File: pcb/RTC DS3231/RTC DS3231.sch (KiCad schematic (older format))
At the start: 9 parts

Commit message: Updated schematic.
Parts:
- added D101: LED, symbol Device:LED
- added D102: D, symbol Device:D
- added R101: 1k, symbol Device:R
- added R102: 200, symbol Device:R
- added RN101: 4.7K, Resistor_THT:R_Array_SIP5, symbol Device:R_Network04_US
- RN102: renamed from RN?; value R_Network04_US -> 4.7K
- gave numbers to parts that had none: 8
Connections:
- net GND: now also BT101.2 (-), J101.6 (Pin_6), J102.4 (Pin_4), JP101.1, JP102.1, JP103.1, U102.7 (WP), D101.1 (K)
- net VCC: now also J101.5 (Pin_5), J102.3 (Pin_3), RN102.1 (common), R101.1, R102.1, RN101.1 (common)
- net 32KHZ: now reaches U101.1 (32KHZ)
- net 32KHZ: now also J101.1 (Pin_1), RN102.5 (R4)
- net VBAT: now reaches U101.14 (VBAT)
- net VBAT: now also BT101.1 (+), D102.1 (K)
- net SDA: now reaches U101.15 (SDA)
- net SDA: now also J101.4 (Pin_4), J102.2 (Pin_2), RN102.2 (R1), U102.6 (SCL)
- net SCL: now reaches U101.16 (SCL)
- net SCL: now also J101.3 (Pin_3), J102.1 (Pin_1), RN102.3 (R2), U102.5 (SDA)
- net SQW: now reaches U101.3 (~INT~/SQW)
- net SQW: now also J101.2 (Pin_2), RN102.4 (R3)
- net at U102.1 (A0): now also JP101.2, RN101.5 (R4)
- net at U102.2 (A1): now also JP102.2, RN101.4 (R3)
- net at U102.3 (A2): now also JP103.2, RN101.3 (R2)
- new net: D101.2 (A), R101.2
- new net: D102.2 (A), R102.2
- no-connect marks 0 -> 2
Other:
- note added: "Battery Charge Circuit"
- moved on the sheet: BT101, J101, J102, JP101, JP102, JP103, RN102, U102

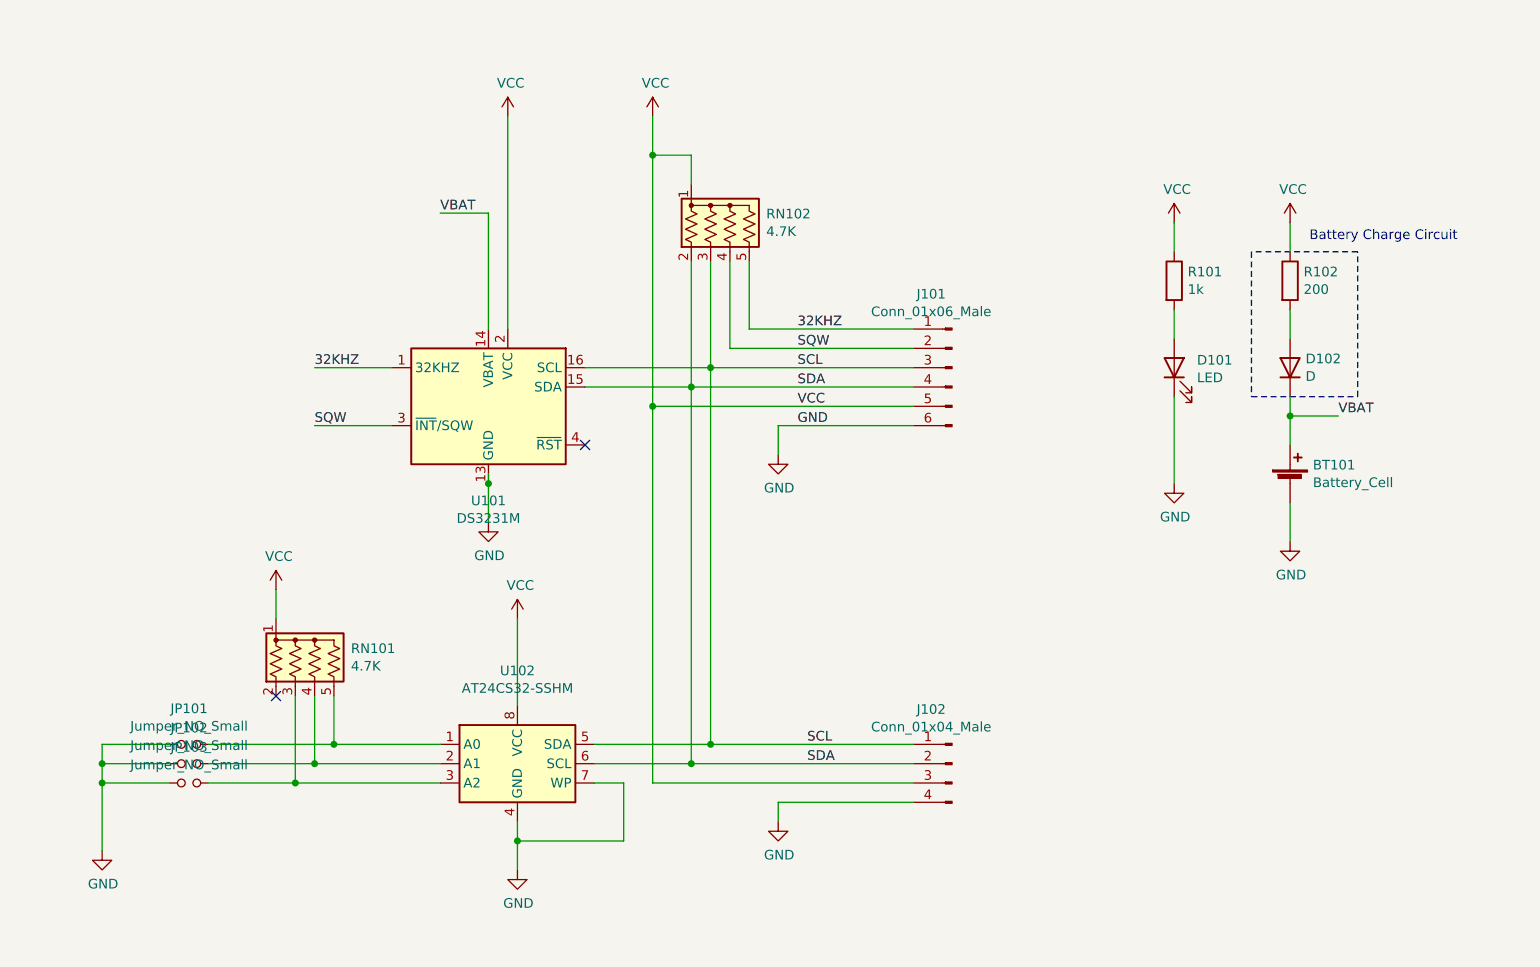
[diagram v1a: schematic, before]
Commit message: Updates schematic to pass ERC.
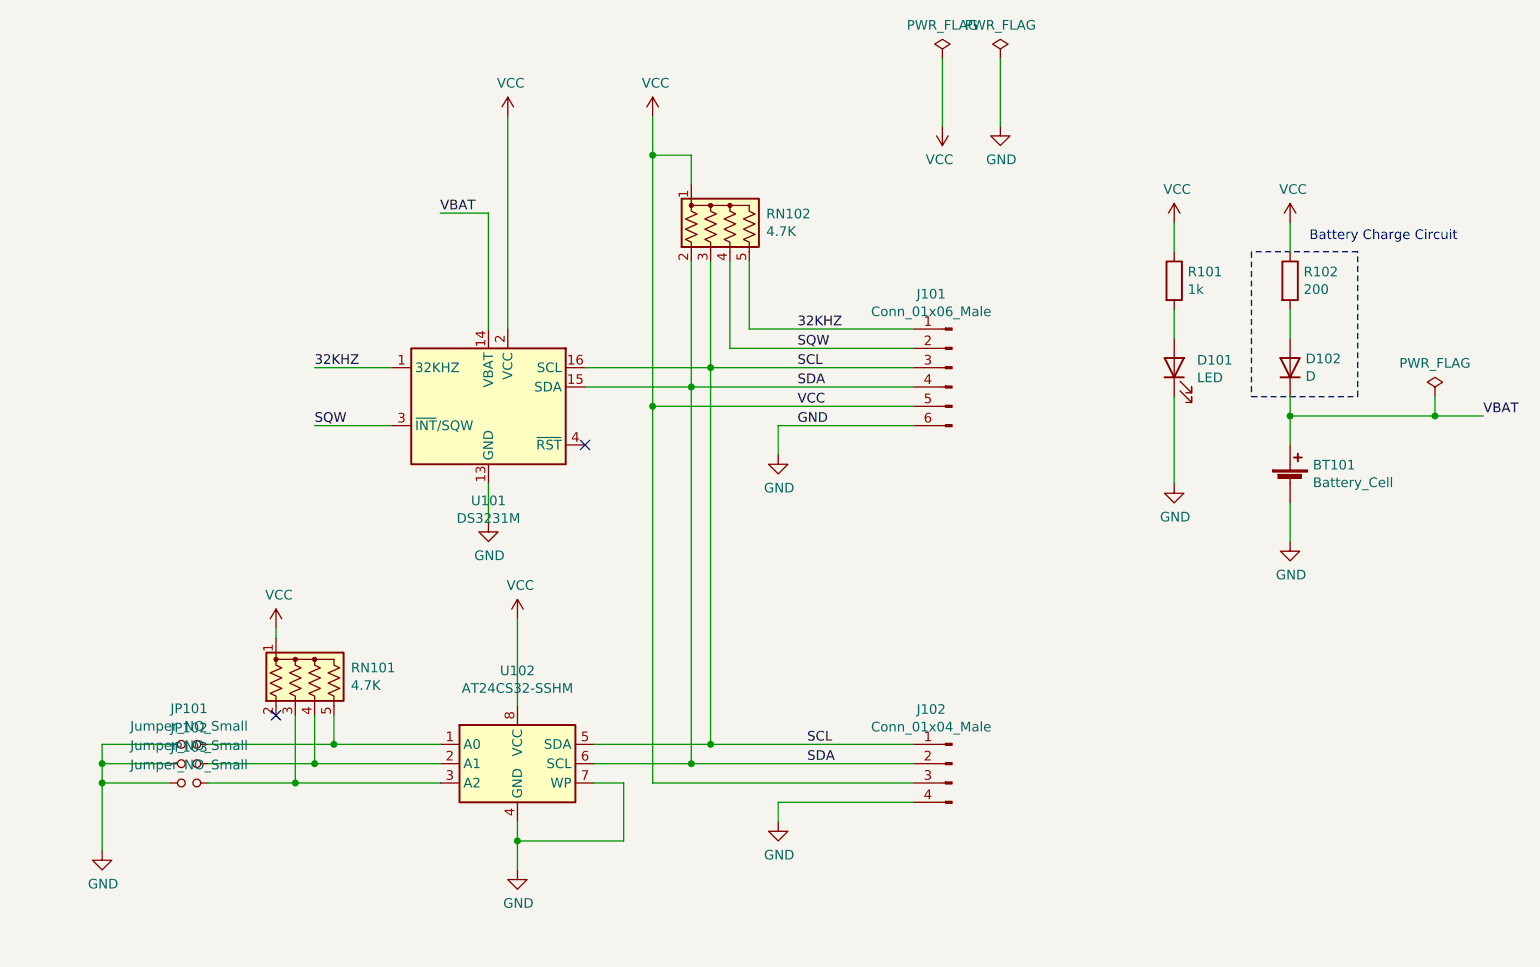
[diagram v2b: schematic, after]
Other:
- moved on the sheet: RN101
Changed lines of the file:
@@
 	-1   0    0    -1
 $EndComp
-Wire Wire Line
-	5250 3800 5250 3600
 $Comp
 L power:GND #PWR0106
@@
 $EndComp
 Wire Wire Line
-	9650 3250 9400 3250
+	10400 3250 10150 3250
 Connection ~ 9400 3250
 Wire Wire Line
@@
 	1    0    0    -1
 $EndComp
-Wire Wire Line
-	9400 2250 9400 2400
 Wire Wire Line
 	9400 2700 9400 2850
@@
 L Device:R_Network04_US RN101
 U 1 1 614AB9B7
-P 4350 4500
-F 0 "RN101" H 4538 4546 50  0000 L CNN
-F 1 "4.7K" H 4538 4455 50  0000 L CNN
-F 2 "Resistor_THT:R_Array_SIP5" V 4625 4500 50  0001 C CNN
-F 3 "http://www.vishay.com/docs/31509/csc.pdf" H 4350 4500 50  0001 C CNN
-	1    4350 4500
+P 4350 4600
+F 0 "RN101" H 4538 4646 50  0000 L CNN
+F 1 "4.7K" H 4538 4555 50  0000 L CNN
+F 2 "Resistor_THT:R_Array_SIP5" V 4625 4600 50  0001 C CNN
+F 3 "http://www.vishay.com/docs/31509/csc.pdf" H 4350 4600 50  0001 C CNN
+	1    4350 4600
 	1    0    0    -1
 $EndComp
@@
 	6750 3300 7450 3300
 Wire Wire Line
-	4150 4150 4150 4300
-Wire Wire Line
-	4450 4700 4450 4950
+	4150 4350 4150 4400
+Wire Wire Line
+	4450 4800 4450 4950
 Wire Wire Line
 	4450 4950 5000 4950
 Wire Wire Line
-	4350 4700 4350 5050
+	4350 4800 4350 5050
 Wire Wire Line
 	4350 5050 5000 5050
 Wire Wire Line
-	4250 4700 4250 5150
+	4250 4800 4250 5150
 Wire Wire Line
 	4250 5150 5000 5150
@@
 Text Label 4350 3300 0    50   ~ 0
 SQW
-Connection ~ 5250 3600
-Wire Wire Line
-	5250 3600 5250 3550
 Wire Wire Line
 	5800 5050 6300 5050
@@
 Wire Wire Line
 	6750 5250 6750 5350
-NoConn ~ 4150 4700
+NoConn ~ 4150 4800
 Wire Wire Line
 	4450 4950 3800 4950
@@
 Wire Wire Line
 	6100 1700 6100 1900
-Wire Wire Line
-	8800 2250 8800 2400
 Text Label 6850 3200 0    50   ~ 0
 VCC
@@
 Text Label 5000 2200 0    50   ~ 0
 VBAT
-Text Label 9650 3250 0    50   ~ 0
+Text Label 10400 3250 0    50   ~ 0
 VBAT
 $Comp
 L power:VCC #PWR0102
 U 1 1 615184B8
-P 4150 4150
-F 0 "#PWR0102" H 4150 4000 50  0001 C CNN
-F 1 "VCC" H 4165 4323 50  0000 C CNN
-F 2 "" H 4150 4150 50  0001 C CNN
-F 3 "" H 4150 4150 50  0001 C CNN
-	1    4150 4150
-	1    0    0    -1
-$EndComp
+P 4150 4350
+F 0 "#PWR0102" H 4150 4200 50  0001 C CNN
+F 1 "VCC" H 4165 4523 50  0000 C CNN
+F 2 "" H 4150 4350 50  0001 C CNN
+F 3 "" H 4150 4350 50  0001 C CNN
+	1    4150 4350
+	1    0    0    -1
+$EndComp
+Wire Wire Line
+	5250 3600 5250 3800
+Wire Wire Line
+	8800 2250 8800 2400
+Wire Wire Line
+	9400 2250 9400 2400
+$Comp
+L power:PWR_FLAG #FLG0101
+U 1 1 6153FCF3
+P 7600 1400
+F 0 "#FLG0101" H 7600 1475 50  0001 C CNN
+F 1 "PWR_FLAG" H 7600 1573 50  0000 C CNN
+F 2 "" H 7600 1400 50  0001 C CNN
+F 3 "~" H 7600 1400 50  0001 C CNN
+	1    7600 1400
+	1    0    0    -1
+$EndComp
+$Comp
+L power:VCC #PWR0114
+U 1 1 6154015D
+P 7600 1750
+F 0 "#PWR0114" H 7600 1600 50  0001 C CNN
+F 1 "VCC" H 7615 1923 50  0000 C CNN
+F 2 "" H 7600 1750 50  0001 C CNN
+F 3 "" H 7600 1750 50  0001 C CNN
+	1    7600 1750
+	-1   0    0    1
+$EndComp
+Wire Wire Line
+	7600 1400 7600 1750
+$Comp
+L power:GND #PWR0115
+U 1 1 615482DE
+P 7900 1750
+F 0 "#PWR0115" H 7900 1500 50  0001 C CNN
+F 1 "GND" H 7905 1577 50  0000 C CNN
+F 2 "" H 7900 1750 50  0001 C CNN
+F 3 "" H 7900 1750 50  0001 C CNN
+	1    7900 1750
+	1    0    0    -1
+$EndComp
+$Comp
+L power:PWR_FLAG #FLG0102
+U 1 1 615486C4
+P 7900 1400
+F 0 "#FLG0102" H 7900 1475 50  0001 C CNN
+F 1 "PWR_FLAG" H 7900 1573 50  0000 C CNN
+F 2 "" H 7900 1400 50  0001 C CNN
+F 3 "~" H 7900 1400 50  0001 C CNN
+	1    7900 1400
+	1    0    0    -1
+$EndComp
+Wire Wire Line
+	7900 1400 7900 1750
+$Comp
+L power:PWR_FLAG #FLG0103
+U 1 1 6154BD34
+P 10150 3150
+F 0 "#FLG0103" H 10150 3225 50  0001 C CNN
+F 1 "PWR_FLAG" H 10150 3323 50  0000 C CNN
+F 2 "" H 10150 3150 50  0001 C CNN
+F 3 "~" H 10150 3150 50  0001 C CNN
+	1    10150 3150
+	1    0    0    -1
+$EndComp
+Wire Wire Line
+	10150 3150 10150 3250
+Connection ~ 10150 3250
+Wire Wire Line
+	10150 3250 9400 3250
 $EndSCHEMATC

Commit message: Modified folders.
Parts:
- BT101: footprint (none) -> Battery:BatteryHolder_Keystone_1058_1x2032
- D101: footprint (none) -> LED_SMD:LED_0402_1005Metric
- D102: footprint (none) -> Diode_SMD:D_0805_2012Metric
- R101, R102: footprint (none) -> Resistor_SMD:R_0805_2012Metric
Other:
- note added: "Power led"
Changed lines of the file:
@@
 F 0 "BT101" H 9518 3696 50  0000 L CNN
 F 1 "Battery_Cell" H 9518 3605 50  0000 L CNN
-F 2 "" V 9400 3660 50  0001 C CNN
+F 2 "Battery:BatteryHolder_Keystone_1058_1x2032" V 9400 3660 50  0001 C CNN
 F 3 "~" V 9400 3660 50  0001 C CNN
 	1    9400 3600
@@
 L power:GND #PWR0106
 U 1 1 6142B186
-P 5400 5600
-F 0 "#PWR0106" H 5400 5350 50  0001 C CNN
-F 1 "GND" H 5405 5427 50  0000 C CNN
-F 2 "" H 5400 5600 50  0001 C CNN
-F 3 "" H 5400 5600 50  0001 C CNN
-	1    5400 5600
+P 5400 5800
+F 0 "#PWR0106" H 5400 5550 50  0001 C CNN
+F 1 "GND" H 5405 5627 50  0000 C CNN
+F 2 "" H 5400 5800 50  0001 C CNN
+F 3 "" H 5400 5800 50  0001 C CNN
+	1    5400 5800
 	1    0    0    -1
 $EndComp
@@
 F 0 "R101" H 8870 2596 50  0000 L CNN
 F 1 "1k" H 8870 2505 50  0000 L CNN
-F 2 "" V 8730 2550 50  0001 C CNN
+F 2 "Resistor_SMD:R_0805_2012Metric" V 8730 2550 50  0001 C CNN
 F 3 "~" H 8800 2550 50  0001 C CNN
 	1    8800 2550
@@
 F 0 "D101" V 8839 2882 50  0000 R CNN
 F 1 "LED" V 8748 2882 50  0000 R CNN
-F 2 "" H 8800 3000 50  0001 C CNN
+F 2 "LED_SMD:LED_0402_1005Metric" H 8800 3000 50  0001 C CNN
 F 3 "~" H 8800 3000 50  0001 C CNN
 	1    8800 3000
@@
 F 0 "D102" V 9446 2920 50  0000 R CNN
 F 1 "D" V 9355 2920 50  0000 R CNN
-F 2 "" H 9400 3000 50  0001 C CNN
+F 2 "Diode_SMD:D_0805_2012Metric" H 9400 3000 50  0001 C CNN
 F 3 "~" H 9400 3000 50  0001 C CNN
 	1    9400 3000
@@
 F 0 "R102" H 9470 2596 50  0000 L CNN
 F 1 "200" H 9470 2505 50  0000 L CNN
-F 2 "" V 9330 2550 50  0001 C CNN
+F 2 "Resistor_SMD:R_0805_2012Metric" V 9330 2550 50  0001 C CNN
 F 3 "~" H 9400 2550 50  0001 C CNN
 	1    9400 2550
@@
 SDA
 Wire Wire Line
-	5000 2200 5250 2200
-Wire Wire Line
-	5250 2200 5250 2800
+	5000 1850 5250 1850
 Wire Wire Line
 	4750 3000 4350 3000
@@
 L power:GND #PWR0109
 U 1 1 614F145B
-P 6750 5350
-F 0 "#PWR0109" H 6750 5100 50  0001 C CNN
-F 1 "GND" H 6755 5177 50  0000 C CNN
-F 2 "" H 6750 5350 50  0001 C CNN
-F 3 "" H 6750 5350 50  0001 C CNN
-	1    6750 5350
+P 6750 5800
+F 0 "#PWR0109" H 6750 5550 50  0001 C CNN
+F 1 "GND" H 6755 5627 50  0000 C CNN
+F 2 "" H 6750 5800 50  0001 C CNN
+F 3 "" H 6750 5800 50  0001 C CNN
+	1    6750 5800
 	1    0    0    -1
 $EndComp
@@
 	7450 5250 6750 5250
 Wire Wire Line
-	6750 5250 6750 5350
+	6750 5250 6750 5800
 NoConn ~ 4150 4800
 Wire Wire Line
@@
 L power:GND #PWR0101
 U 1 1 614FD842
-P 3250 5500
-F 0 "#PWR0101" H 3250 5250 50  0001 C CNN
-F 1 "GND" H 3255 5327 50  0000 C CNN
-F 2 "" H 3250 5500 50  0001 C CNN
-F 3 "" H 3250 5500 50  0001 C CNN
-	1    3250 5500
+P 3250 5800
+F 0 "#PWR0101" H 3250 5550 50  0001 C CNN
+F 1 "GND" H 3255 5627 50  0000 C CNN
+F 2 "" H 3250 5800 50  0001 C CNN
+F 3 "" H 3250 5800 50  0001 C CNN
+	1    3250 5800
 	1    0    0    -1
 $EndComp
@@
 Connection ~ 3250 5150
 Wire Wire Line
-	3250 5150 3250 5500
+	3250 5150 3250 5800
 Wire Wire Line
 	3250 4950 3250 5050
@@
 Connection ~ 5400 5450
 Wire Wire Line
-	5400 5450 5400 5600
+	5400 5450 5400 5800
 NoConn ~ 5750 3400
 $Comp
@@
 Text Label 6850 3300 0    50   ~ 0
 GND
-Text Label 5000 2200 0    50   ~ 0
+Text Label 5000 1850 0    50   ~ 0
 VBAT
 Text Label 10400 3250 0    50   ~ 0
@@
 L power:PWR_FLAG #FLG0101
 U 1 1 6153FCF3
-P 7600 1400
-F 0 "#FLG0101" H 7600 1475 50  0001 C CNN
-F 1 "PWR_FLAG" H 7600 1573 50  0000 C CNN
-F 2 "" H 7600 1400 50  0001 C CNN
-F 3 "~" H 7600 1400 50  0001 C CNN
-	1    7600 1400
+P 3450 2200
+F 0 "#FLG0101" H 3450 2275 50  0001 C CNN
+F 1 "PWR_FLAG" H 3450 2373 50  0000 C CNN
+F 2 "" H 3450 2200 50  0001 C CNN
+F 3 "~" H 3450 2200 50  0001 C CNN
+	1    3450 2200
 	1    0    0    -1
 $EndComp
@@
 L power:VCC #PWR0114
 U 1 1 6154015D
-P 7600 1750
-F 0 "#PWR0114" H 7600 1600 50  0001 C CNN
-F 1 "VCC" H 7615 1923 50  0000 C CNN
-F 2 "" H 7600 1750 50  0001 C CNN
-F 3 "" H 7600 1750 50  0001 C CNN
-	1    7600 1750
+P 3450 2550
+F 0 "#PWR0114" H 3450 2400 50  0001 C CNN
+F 1 "VCC" H 3465 2723 50  0000 C CNN
+F 2 "" H 3450 2550 50  0001 C CNN
+F 3 "" H 3450 2550 50  0001 C CNN
+	1    3450 2550
 	-1   0    0    1
 $EndComp
 Wire Wire Line
-	7600 1400 7600 1750
+	3450 2200 3450 2550
 $Comp
 L power:GND #PWR0115
 U 1 1 615482DE
-P 7900 1750
-F 0 "#PWR0115" H 7900 1500 50  0001 C CNN
-F 1 "GND" H 7905 1577 50  0000 C CNN
-F 2 "" H 7900 1750 50  0001 C CNN
-F 3 "" H 7900 1750 50  0001 C CNN
-	1    7900 1750
+P 3750 2550
+F 0 "#PWR0115" H 3750 2300 50  0001 C CNN
+F 1 "GND" H 3755 2377 50  0000 C CNN
+F 2 "" H 3750 2550 50  0001 C CNN
+F 3 "" H 3750 2550 50  0001 C CNN
+	1    3750 2550
 	1    0    0    -1
 $EndComp
@@
 L power:PWR_FLAG #FLG0102
 U 1 1 615486C4
-P 7900 1400
-F 0 "#FLG0102" H 7900 1475 50  0001 C CNN
-F 1 "PWR_FLAG" H 7900 1573 50  0000 C CNN
-F 2 "" H 7900 1400 50  0001 C CNN
-F 3 "~" H 7900 1400 50  0001 C CNN
-	1    7900 1400
-	1    0    0    -1
-$EndComp
-Wire Wire Line
-	7900 1400 7900 1750
+P 3750 2200
+F 0 "#FLG0102" H 3750 2275 50  0001 C CNN
+F 1 "PWR_FLAG" H 3750 2373 50  0000 C CNN
+F 2 "" H 3750 2200 50  0001 C CNN
+F 3 "~" H 3750 2200 50  0001 C CNN
+	1    3750 2200
+	1    0    0    -1
+$EndComp
+Wire Wire Line
+	3750 2200 3750 2550
 $Comp
 L power:PWR_FLAG #FLG0103
@@
 Wire Wire Line
 	10150 3250 9400 3250
+Wire Wire Line
+	5250 1850 5250 2800
+Wire Notes Line
+	8650 2350 8650 3350
+Wire Notes Line
+	8650 3350 9150 3350
+Wire Notes Line
+	9150 3350 9150 2350
+Wire Notes Line
+	9150 2350 8650 2350
+Text Notes 8850 2300 0    50   ~ 0
+Power led
 $EndSCHEMATC
